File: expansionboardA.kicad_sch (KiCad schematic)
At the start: 60 parts, among them J1 DEBUG, J2 USB_A_Stacked, J3 HDMI_A, J4 FAN, P1 USB_C_Plug, U1 MAX3420EECJ, U2 GPIO_U2, U3 AMS1117-3.3, U4 GPIO_U4, U5 MCP3008T-I/SL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

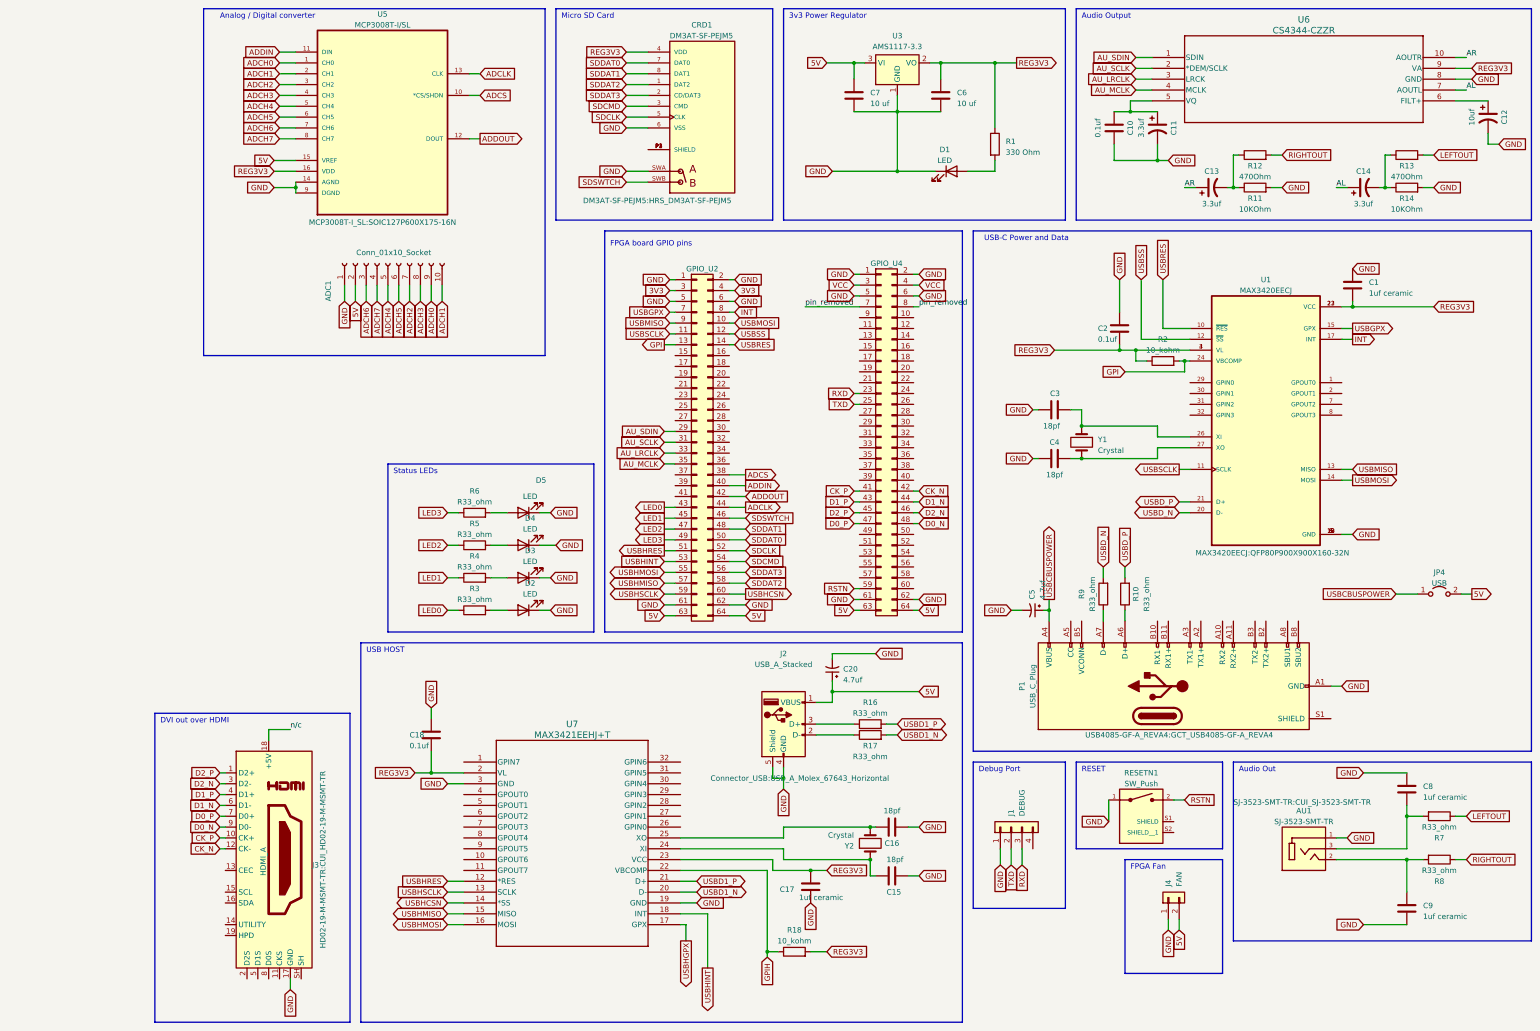
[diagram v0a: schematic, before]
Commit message: Some modifications for mount holes and expansion port Also added optional pullup resistors
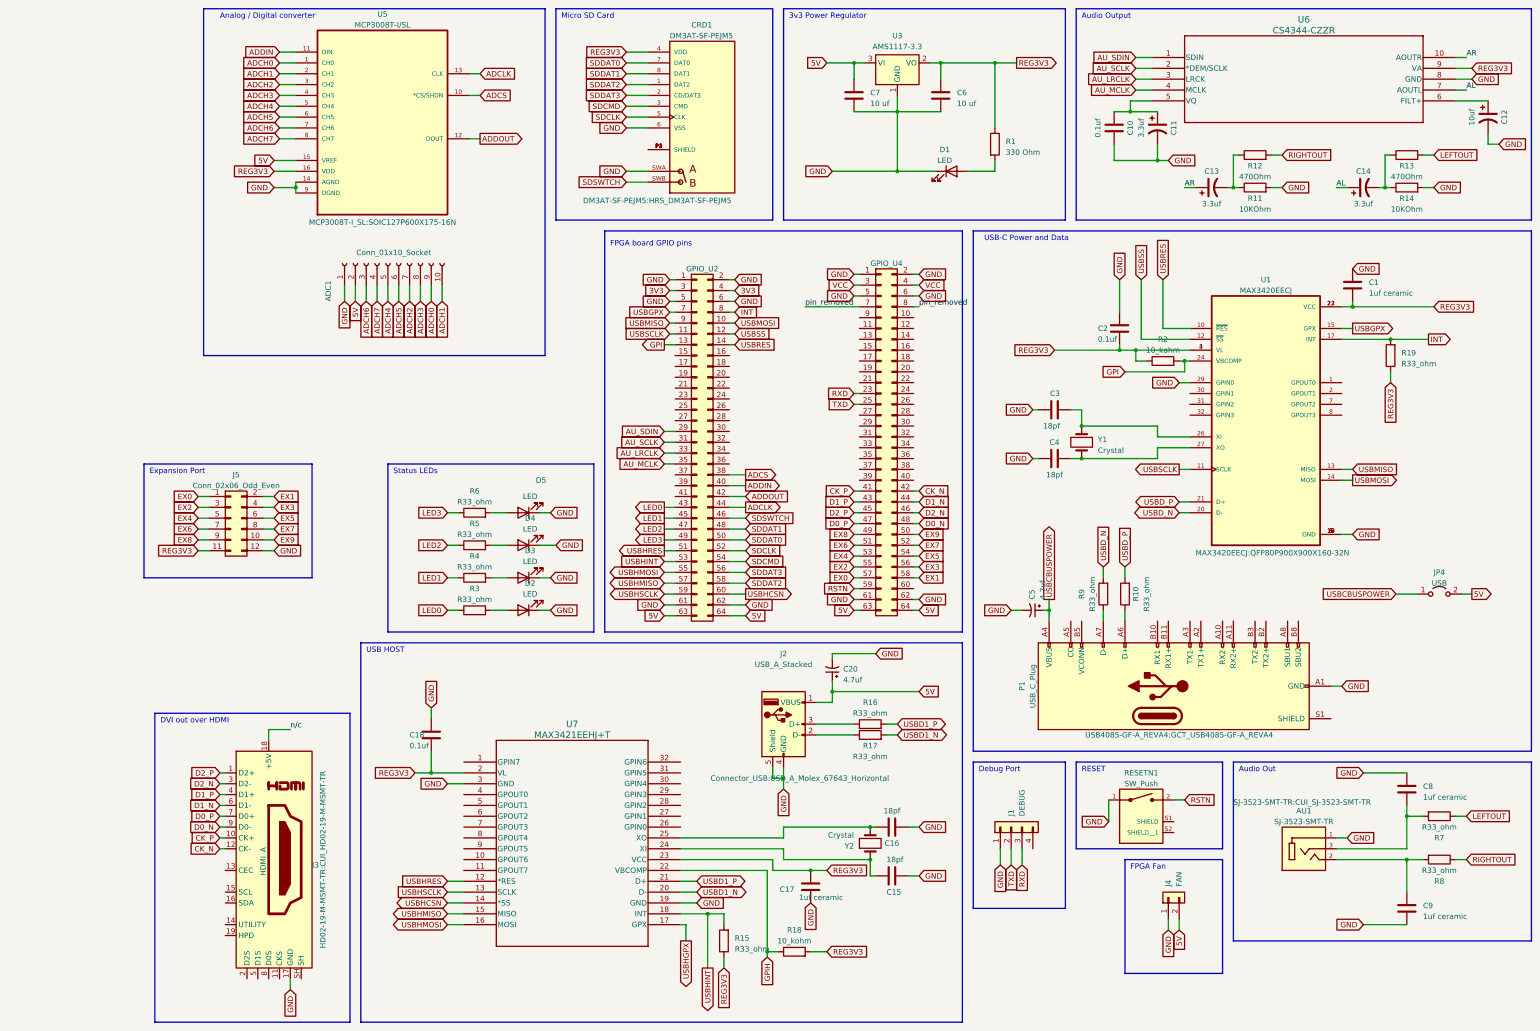
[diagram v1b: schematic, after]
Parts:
- added J5: Conn_02x06_Odd_Even, Connector_PinSocket_2.54mm:PinSocket_2x06_P2.54mm_Vertical, symbol Connector_Generic:Conn_02x06_Odd_Even
- added R15, R19: R33_ohm, Resistor_SMD:R_0603_1608Metric_Pad0.98x0.95mm_HandSolder, symbol Device:R
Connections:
- net GND: now also U1.29 (GPIN0), J5.12 (Pin_12)
- net INT: now also R19.2
- net REG3V3: now also J5.11 (Pin_11), R15.1, R19.1
- net USBHINT: now also R15.2
- net EX8: now reaches U4.49 (Pin_49)
- net EX8: now also J5.9 (Pin_9)
- net EX9: now reaches U4.50 (Pin_50)
- net EX9: now also J5.10 (Pin_10)
- net EX6: now reaches U4.51 (Pin_51)
- net EX6: now also J5.7 (Pin_7)
- net EX7: now reaches U4.52 (Pin_52)
- net EX7: now also J5.8 (Pin_8)
- net EX4: now reaches U4.53 (Pin_53)
- net EX4: now also J5.5 (Pin_5)
- net EX5: now reaches U4.54 (Pin_54)
- net EX5: now also J5.6 (Pin_6)
- net EX2: now reaches U4.55 (Pin_55)
- net EX2: now also J5.3 (Pin_3)
- net EX3: now reaches U4.56 (Pin_56)
- net EX3: now also J5.4 (Pin_4)
- net EX0: now reaches U4.57 (Pin_57)
- net EX0: now also J5.1 (Pin_1)
- net EX1: now reaches U4.58 (Pin_58)
- net EX1: now also J5.2 (Pin_2)
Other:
- note added: "Expansion Port"

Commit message: Updated board
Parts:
- added J6: Conn_02x06_Odd_Even, Connector_PinSocket_2.54mm:PinSocket_2x06_P2.54mm_Vertical, symbol Connector_Generic:Conn_02x06_Odd_Even
- added J7: DEBUG, Connector_PinSocket_2.54mm:PinSocket_1x04_P2.54mm_Vertical, symbol Connector_Generic:Conn_01x04
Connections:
- net GND: now also J6.12 (Pin_12), J7.1 (Pin_1)
- net REG3V3: now also J6.11 (Pin_11)
- net RXD2: now reaches U4.24 (Pin_24)
- net RXD2: now also J7.3 (Pin_3)
- net TXD2: now reaches U4.26 (Pin_26)
- net TXD2: now also J7.2 (Pin_2)
- net EX18: now reaches U4.31 (Pin_31)
- net EX18: now also J6.10 (Pin_10)
- net EX19: now reaches U4.32 (Pin_32)
- net EX19: now also J6.9 (Pin_9)
- net EX16: now reaches U4.33 (Pin_33)
- net EX16: now also J6.8 (Pin_8)
- net EX17: now reaches U4.34 (Pin_34)
- net EX17: now also J6.7 (Pin_7)
- net EX14: now reaches U4.35 (Pin_35)
- net EX14: now also J6.6 (Pin_6)
- net EX15: now reaches U4.36 (Pin_36)
- net EX15: now also J6.5 (Pin_5)
- net EX12: now reaches U4.37 (Pin_37)
- net EX12: now also J6.4 (Pin_4)
- net EX13: now reaches U4.38 (Pin_38)
- net EX13: now also J6.3 (Pin_3)
- net EX10: now reaches U4.39 (Pin_39)
- net EX10: now also J6.2 (Pin_2)
- net EX11: now reaches U4.40 (Pin_40)
- net EX11: now also J6.1 (Pin_1)
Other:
- note added: "Expansion Port A"
- note added: "Expansion Port B"
- note added: "UART Port A"
- note added: "UART Port B"
- note removed: "Debug Port"
- note removed: "Expansion Port"
- moved on the sheet: J1, J4, J5, R15

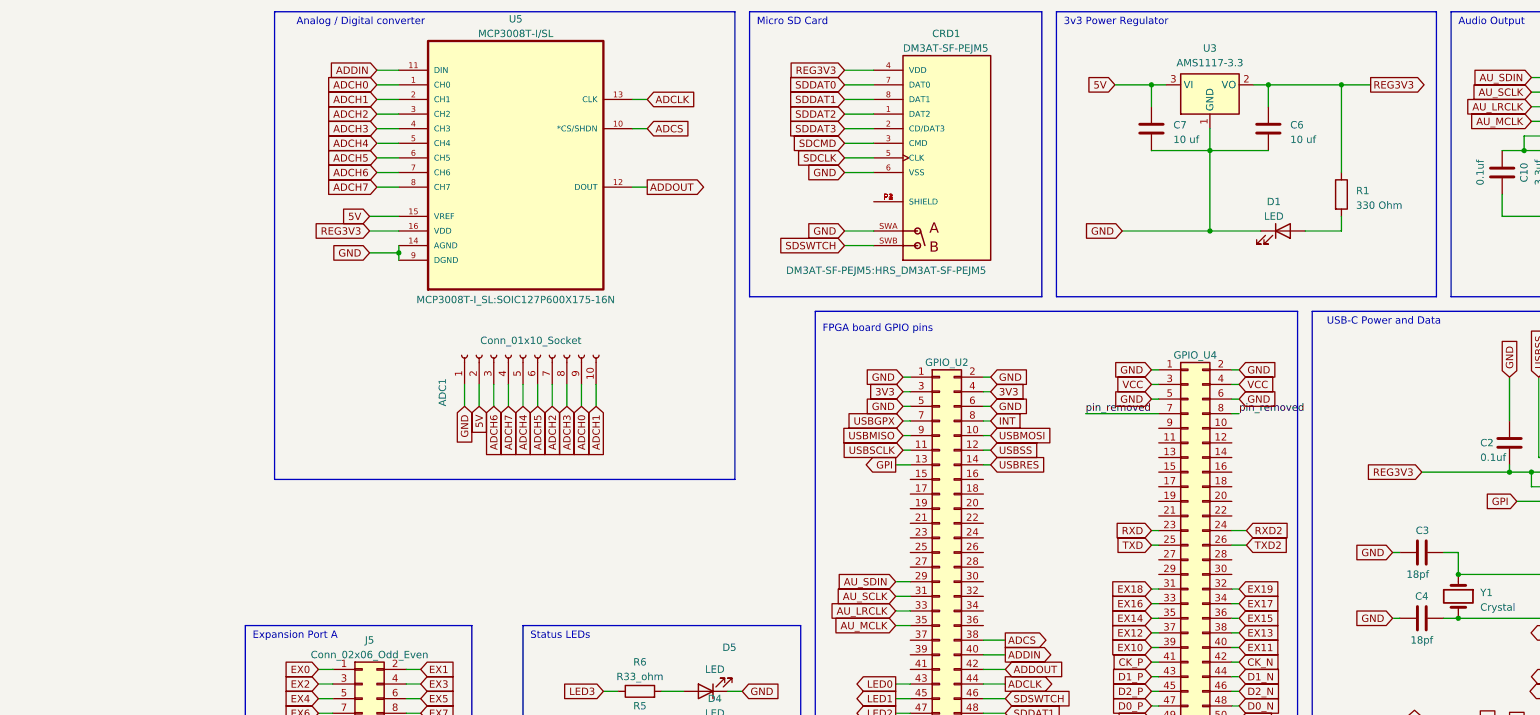
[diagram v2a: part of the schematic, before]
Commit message: Updated board file with new power regulator
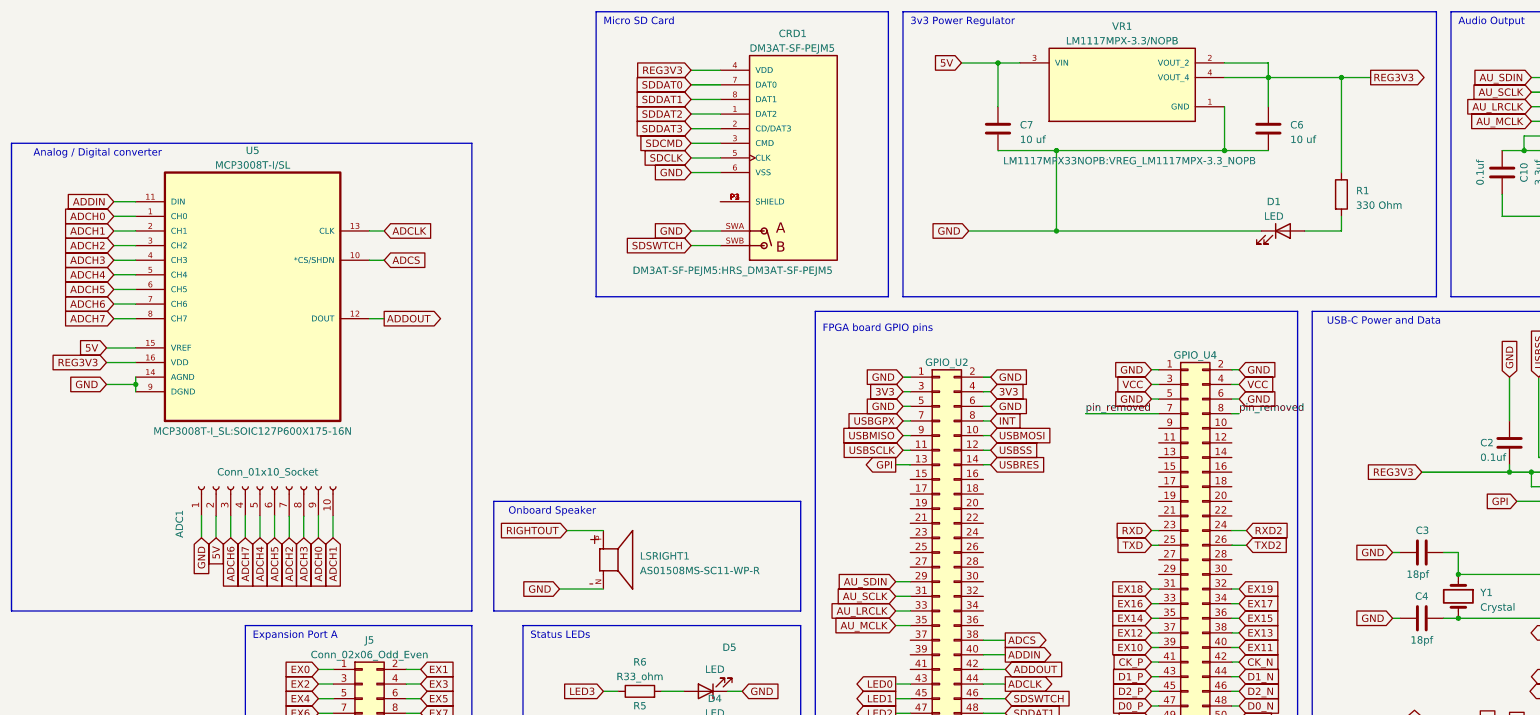
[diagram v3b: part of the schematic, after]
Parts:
- removed U3: AMS1117-3.3, Package_TO_SOT_SMD:SOT-89-3_Handsoldering, symbol Regulator_Linear:AMS1117-3.3
- added LSRIGHT1: AS01508MS-SC11-WP-R, SPKR_AS01508MS-SC11-WP-R, symbol AS01508MS-SC11-WP-R:AS01508MS-SC11-WP-R
- added VR1: LM1117MPX-3.3/NOPB, LM1117MPX33NOPB:VREG_LM1117MPX-3.3_NOPB, symbol LM1117MPX-3.3_NOPB:LM1117MPX-3.3/NOPB
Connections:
- net 5V: now also VR1.3 (VIN)
- net GND: now also LSRIGHT1.N, VR1.1 (GND)
- net REG3V3: now also VR1.2 (VOUT_2), VR1.4 (VOUT_4)
- net RIGHTOUT: now also LSRIGHT1.P
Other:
- note added: "Onboard Speaker"
- moved on the sheet: ADC1, C7, CRD1, U5

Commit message: mods
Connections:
- net pin_removed renamed N/C
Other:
- moved on the sheet: ADC1, D2, D3, D4, D5, J5, J6, LSRIGHT1, R3, R4, R5, R6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

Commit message: Updated board
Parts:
- removed J7: DEBUG, Connector_PinSocket_2.54mm:PinSocket_1x04_P2.54mm_Vertical, symbol Connector_Generic:Conn_01x04
- added R20: R33_ohm, Resistor_SMD:R_0603_1608Metric_Pad0.98x0.95mm_HandSolder, symbol Device:R
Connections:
- net 5V: now also R20.2
- net PWMn: now reaches U4.60 (Pin_60)
- net PWMn: now also R20.1
- net RXD2: no longer names the net of U4.24 (Pin_24)
- net TXD2: no longer names the net of U4.26 (Pin_26)
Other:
- note removed: "UART Port B"
- moved on the sheet: J4
